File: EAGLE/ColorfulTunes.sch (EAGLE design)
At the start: 6 parts, among them U1 0.56_HEX_BACKPACK

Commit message: Please check this schematic :)
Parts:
- added CS1: COLOR_SENSOR_PINS, ColorfulTunes:COLOR_SENSOR_PINS
- added R4, R5, R6, R7: (no value), ColorfulTunes:R_R0402
- added R8: POTENTIOMETER, ColorfulTunes:POTENTIOMETER
- added SERVO1: SERVO_PINS, ColorfulTunes:SERVO_PINS
- added USB1: USB_BOI, ColorfulTunes:USB_BOI
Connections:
- removed net RGB_PWR: D1.PWR, U$1.SYS.3V3_1
- new net AIN_1V8.0: R8.S, U$1.AIN_1V8.0
- new net AIN_1V8.REF+: R8.CCW, U$1.AIN.1V8
- new net AIN_1V8.REF-: R8.CW, U$1.AIN_1V8.REF-
- new net GND: CS1.GND, SERVO1.GND, U$1.SYS.GND, U$1.SYS.GND_1, U$1.SYS.GND_3, U$1.SYS_GND_2, U1.GND
- new net I2C1.SCL: CS1.SCL, R7.1, U$1.I2C1.SCL
- new net I2C1.SDA: CS1.SDA, R6.1, U$1.I2C1.SDA
- new net I2C2.SCL: R4.1, U$1.I2C2.SCL, U1.SCL
- new net I2C2.SDA: R5.1, U$1.I2C2.SDA, U1.SDA
- new net N$4: U$1.USB1.VBUS, U$1.USB1.V_EN
- new net SERVO_PWM: SERVO1.SIG, U$1.PWM0
- new net USB1.D+: U$1.USB1.DP, USB1.D+
- new net USB1.D-: U$1.USB1.DN, USB1.D-
- new net USB1.GND: U$1.USB1.GND, U$1.USB1.ID, USB1.GND
- new net USB1.VIN: U$1.USB1.VIN, USB1.5V
- new net VDD_3P3V: D1.PWR, R4.2, R5.2, R6.2, R7.2, U$1.SYS.3V3, U$1.SYS.3V3_1
- new net VDD_5V: CS1.VIN, SERVO1.PWR, U$1.SYS.5V, U$1.SYS.5V_1, U$1.SYS_VIN, U1.VCC
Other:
- note added: "Color Sensor"
- note added: "HEX DISPLAY"
- note added: "POTENTIOMETER"
- note added: "RGB_LED"
- note added: "USB"
- moved on the sheet: D1, R1, R2, R3, U1

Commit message: Found some mistakes, please check this one. Thank you!
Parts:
- R1, R2, R3: value (none) -> 470 M
- R4, R6, R7: value (none) -> 2.2 k
- R5: value (none) -> 2.2k
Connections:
- net VDD_5V: no longer U$1.SYS.5V_1
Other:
- moved on the sheet: R1, R2, R3, R4, R6

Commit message: Am I really done? Is there really justice in this cold dark world?
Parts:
- added SW1: SLIDE_SWITCH, ColorfulTunes:SLIDE_SWITCH
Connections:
- removed net USB1.GND: U$1.USB1.GND, U$1.USB1.ID, USB1.GND
- new net PRU0.6: SW1.COMM, U$1.PRU0.6
- net GND: now also SW1.POS2, U$1.USB1.GND, U$1.USB1.ID, USB1.GND
- net VDD_3P3V: now also SW1.POS1
- net VDD_5V: now also U$1.SYS.5V_1; no longer U$1.SYS_VIN
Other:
- note added: "SWITCH"
- moved on the sheet: SERVO1

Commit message: Almost there!
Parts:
- added FUD1, FUD2, FUD3: FIDUCIAL, ColorfulTunes:FIDUCIAL
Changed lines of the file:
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@@
 <part name="SUPPLY11" library="ColorfulTunes" deviceset="VDD_3P3V" device=""/>
 <part name="GND7" library="ColorfulTunes" deviceset="GND" device=""/>
+<part name="FUD1" library="ColorfulTunes" deviceset="FIDUCIAL" device=""/>
+<part name="FUD2" library="ColorfulTunes" deviceset="FIDUCIAL" device=""/>
+<part name="FUD3" library="ColorfulTunes" deviceset="FIDUCIAL" device=""/>
 </parts>
 <sheets>
@@
 <attribute name="VALUE" x="158.75" y="212.09" size="1.778" layer="96"/>
 </instance>
+<instance part="FUD1" gate="G$1" x="152.4" y="60.96" smashed="yes"/>
+<instance part="FUD2" gate="G$1" x="160.02" y="60.96" smashed="yes"/>
+<instance part="FUD3" gate="G$1" x="167.64" y="60.96" smashed="yes"/>
 </instances>
 <busses>
@@
 </segment>
 <segment>
+<pinref part="U$1" gate="G$1" pin="USB1.GND"/>
+<wire x1="247.65" y1="201.93" x2="243.84" y2="201.93" width="0.1524" layer="91"/>
+<pinref part="GND5" gate="1" pin="GND"/>
 <pinref part="U$1" gate="G$1" pin="USB1.ID"/>
-<pinref part="U$1" gate="G$1" pin="USB1.GND"/>
-<wire x1="247.65" y1="204.47" x2="247.65" y2="201.93" width="0.1524" layer="91"/>
-<wire x1="247.65" y1="201.93" x2="232.41" y2="201.93" width="0.1524" layer="91"/>
-<junction x="247.65" y="201.93"/>
-<pinref part="GND5" gate="1" pin="GND"/>
+<wire x1="243.84" y1="201.93" x2="232.41" y2="201.93" width="0.1524" layer="91"/>
+<wire x1="247.65" y1="204.47" x2="243.84" y2="204.47" width="0.1524" layer="91"/>
+<wire x1="243.84" y1="204.47" x2="243.84" y2="201.93" width="0.1524" layer="91"/>
+<junction x="243.84" y="201.93"/>
 </segment>
 <segment>
@@
 </segment>
 </net>
-<net name="N$4" class="0">
-<segment>
-<pinref part="U$1" gate="G$1" pin="USB1.V_EN"/>
-<pinref part="U$1" gate="G$1" pin="USB1.VBUS"/>
-<wire x1="247.65" y1="217.17" x2="247.65" y2="214.63" width="0.1524" layer="91"/>
-</segment>
-</net>
 <net name="AIN_1V8.0" class="0">
 <segment>
@@
 </segment>
 </net>
+<net name="N$4" class="0">
+<segment>
+<pinref part="U$1" gate="G$1" pin="USB1.V_EN"/>
+<wire x1="247.65" y1="217.17" x2="243.84" y2="217.17" width="0.1524" layer="91"/>
+<wire x1="243.84" y1="217.17" x2="243.84" y2="214.63" width="0.1524" layer="91"/>
+<pinref part="U$1" gate="G$1" pin="USB1.VBUS"/>
+<wire x1="243.84" y1="214.63" x2="247.65" y2="214.63" width="0.1524" layer="91"/>
+</segment>
+</net>

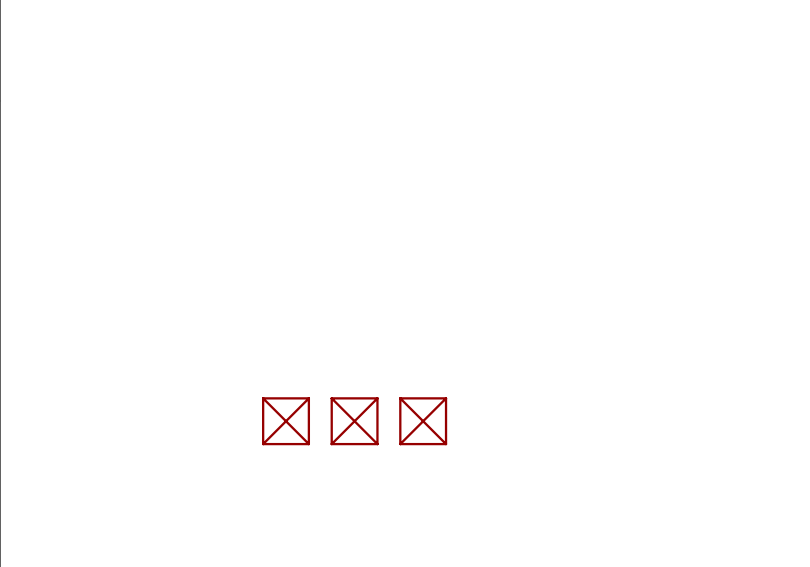
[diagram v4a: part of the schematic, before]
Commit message: with the mounting holes
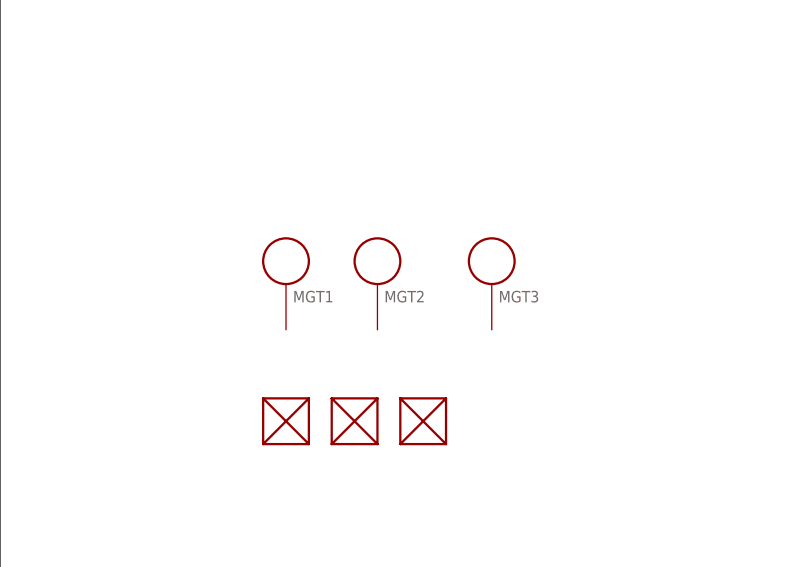
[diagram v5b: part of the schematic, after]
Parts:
- added MGT1, MGT2, MGT3: MOUNTING_HOLE, ColorfulTunes:MOUNTING_HOLE
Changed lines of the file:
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@@
 <part name="FUD2" library="ColorfulTunes" deviceset="FIDUCIAL" device=""/>
 <part name="FUD3" library="ColorfulTunes" deviceset="FIDUCIAL" device=""/>
+<part name="MGT1" library="ColorfulTunes" deviceset="MOUNTING_HOLE" device=""/>
+<part name="MGT2" library="ColorfulTunes" deviceset="MOUNTING_HOLE" device=""/>
+<part name="MGT3" library="ColorfulTunes" deviceset="MOUNTING_HOLE" device=""/>
 </parts>
 <sheets>
@@
 <instance part="FUD2" gate="G$1" x="160.02" y="60.96" smashed="yes"/>
 <instance part="FUD3" gate="G$1" x="167.64" y="60.96" smashed="yes"/>
+<instance part="MGT1" gate="G$1" x="152.4" y="76.2" smashed="yes">
+<attribute name="NAME" x="153.162" y="74.168" size="1.27" layer="95"/>
+</instance>
+<instance part="MGT2" gate="G$1" x="162.56" y="76.2" smashed="yes">
+<attribute name="NAME" x="163.322" y="74.168" size="1.27" layer="95"/>
+</instance>
+<instance part="MGT3" gate="G$1" x="175.26" y="76.2" smashed="yes">
+<attribute name="NAME" x="176.022" y="74.168" size="1.27" layer="95"/>
+</instance>
 </instances>
 <busses>
